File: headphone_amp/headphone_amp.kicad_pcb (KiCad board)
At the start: 2 copper layers, 47.6 x 31.8 mm, 31 parts, among them J1 POWER, J2 INPUT, J3 PHONES, U1 LDL1117S50R, U2 LM4808

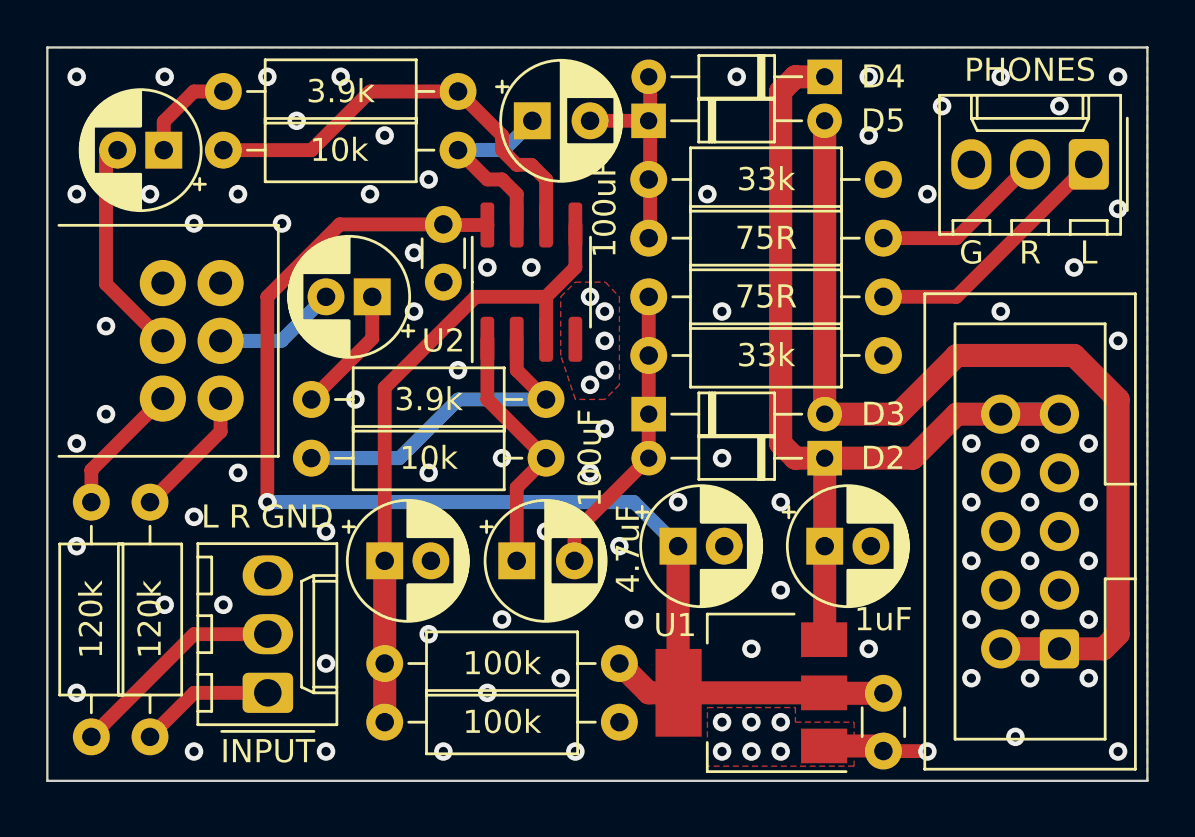
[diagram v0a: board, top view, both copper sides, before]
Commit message: Finish silkscreen. Reexport gerbers
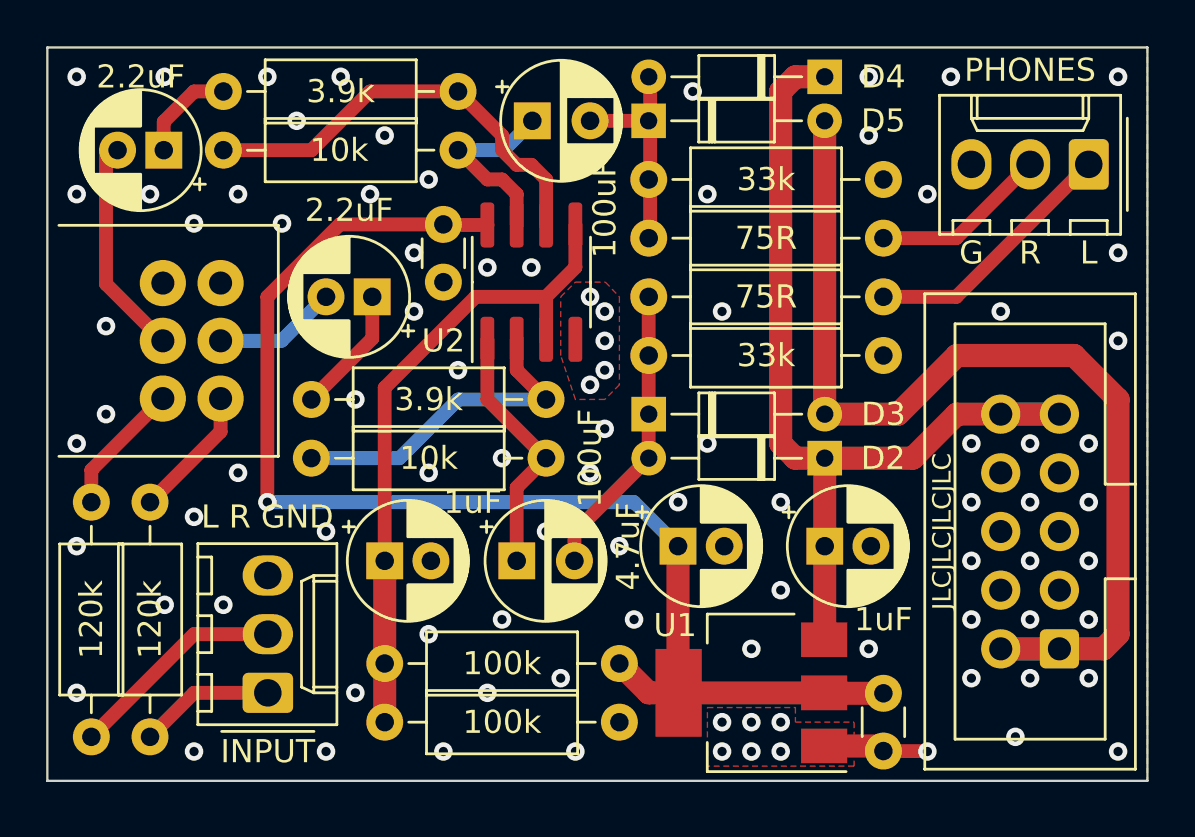
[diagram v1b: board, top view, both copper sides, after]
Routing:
- net GND: vias 97 -> 94
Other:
- board text added: "D2"
- board text added: "D3"
- board text added: "D4"
- board text added: "D5"
- board text added: "INPUT"
- board text added: "JLCJLCJLCJLC"
- board text added: "LM4808 Headphone Amp Max Proskauer v0.1 May 2022"
- board text added: "OUTPUT"

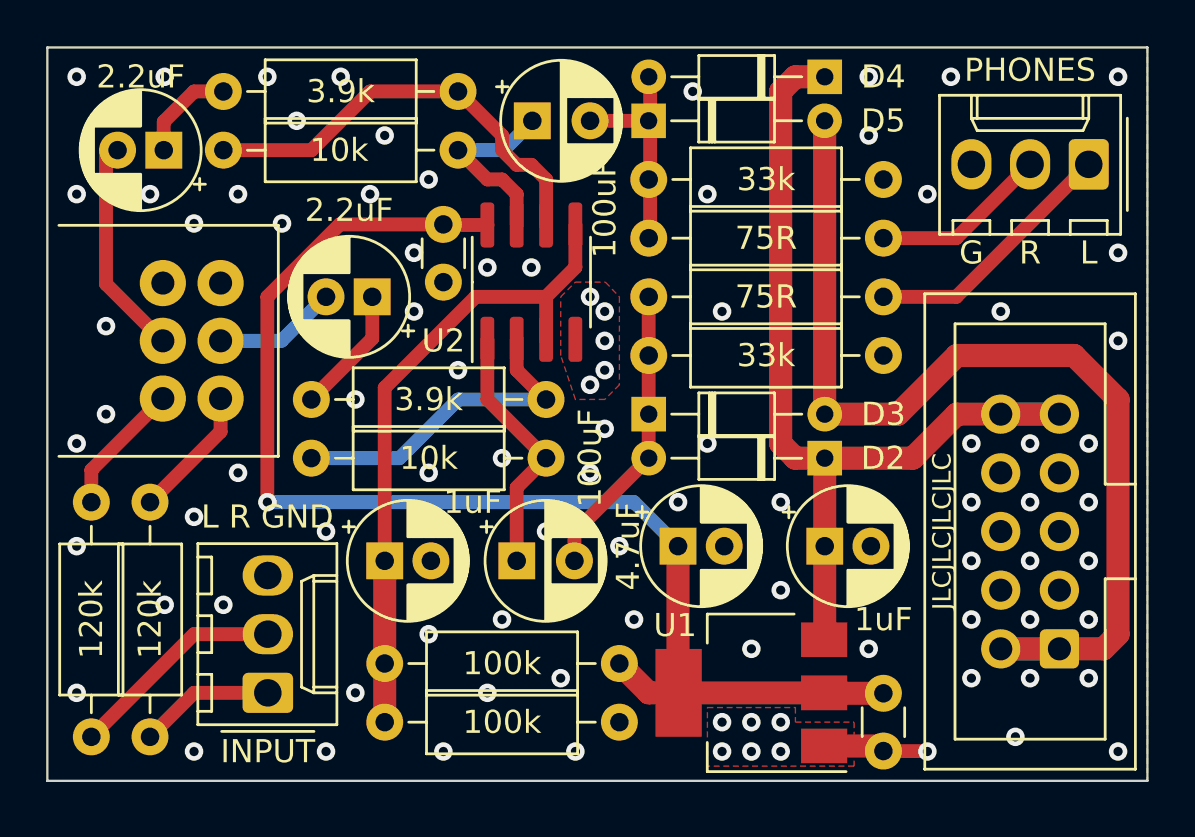
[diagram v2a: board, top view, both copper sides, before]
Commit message: Add mono jumper
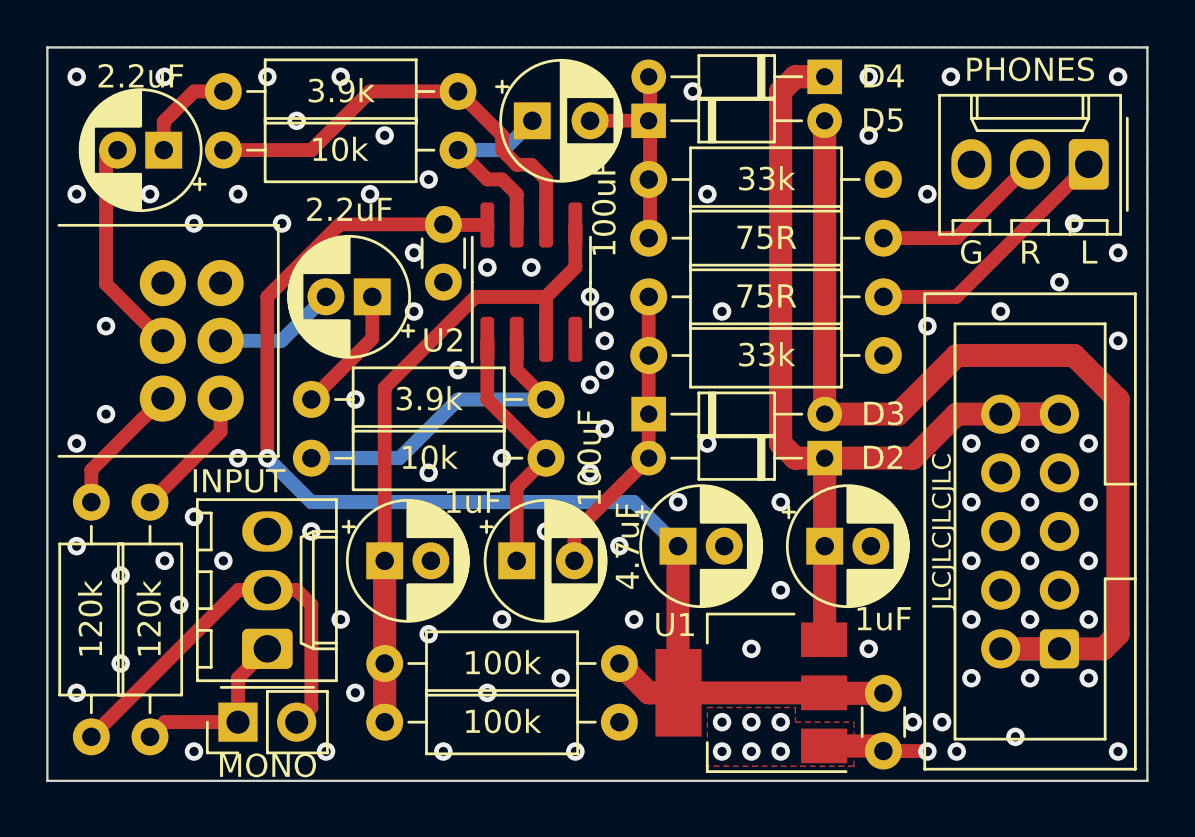
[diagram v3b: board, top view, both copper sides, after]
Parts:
- added JP1: MONO, Connector_PinHeader_2.54mm:PinHeader_1x02_P2.54mm_Vertical, F.Cu at (131.4, 112.4)
- RV1: footprint headphone_amp:Pot_Bourns_PTD902 -> kosmo-lib:Pot_Bourns_PTD902
- moved J2 1.91 mm to (132.7, 109.2)
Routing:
- net /SIG_R: track 9.48 -> 17.8 mm
- net /SIG_L: track 5.89 -> 7.77 mm
- net +5V: track 56.6 -> 55.5 mm
- net GND: vias 94 -> 104
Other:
- board text removed: "L R GND"
